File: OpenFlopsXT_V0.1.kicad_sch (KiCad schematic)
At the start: 69 parts, among them J1 UP, J2 DN, J3 R, J4 G, J5 Conn_01x22_Female, P1 FLOPPY_CONN, P2 POWER_INPUT, P3 POWER_PASSTHRU, P4 PROG_PORT, P6 ENCODER_PORT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

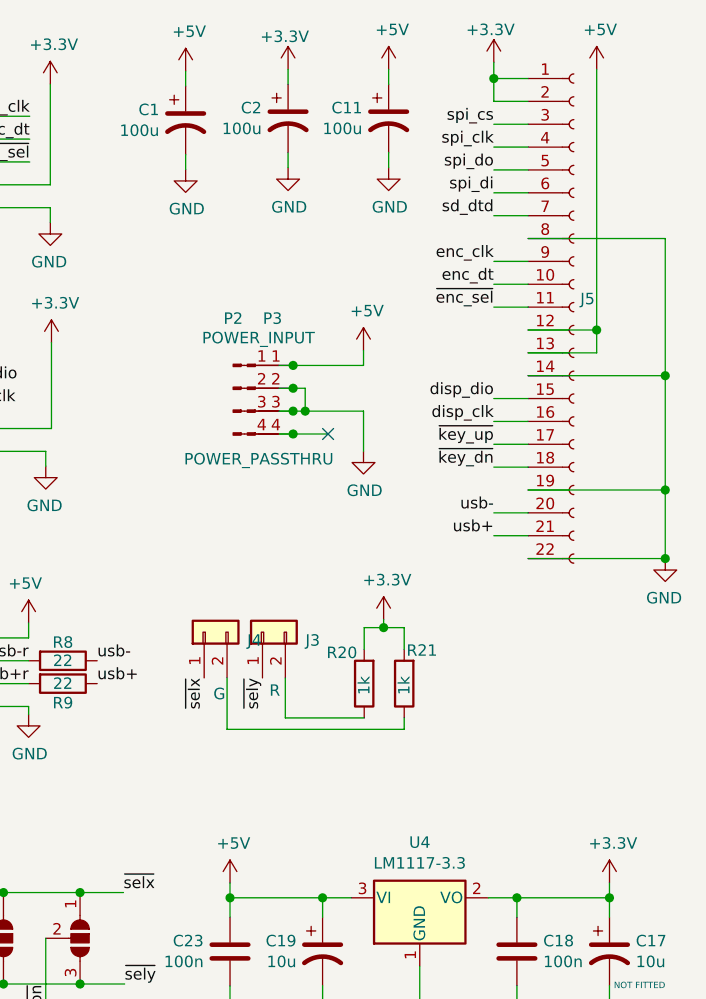
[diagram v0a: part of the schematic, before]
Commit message: Upgraded Flat Flex Connector OpenFlopsXT
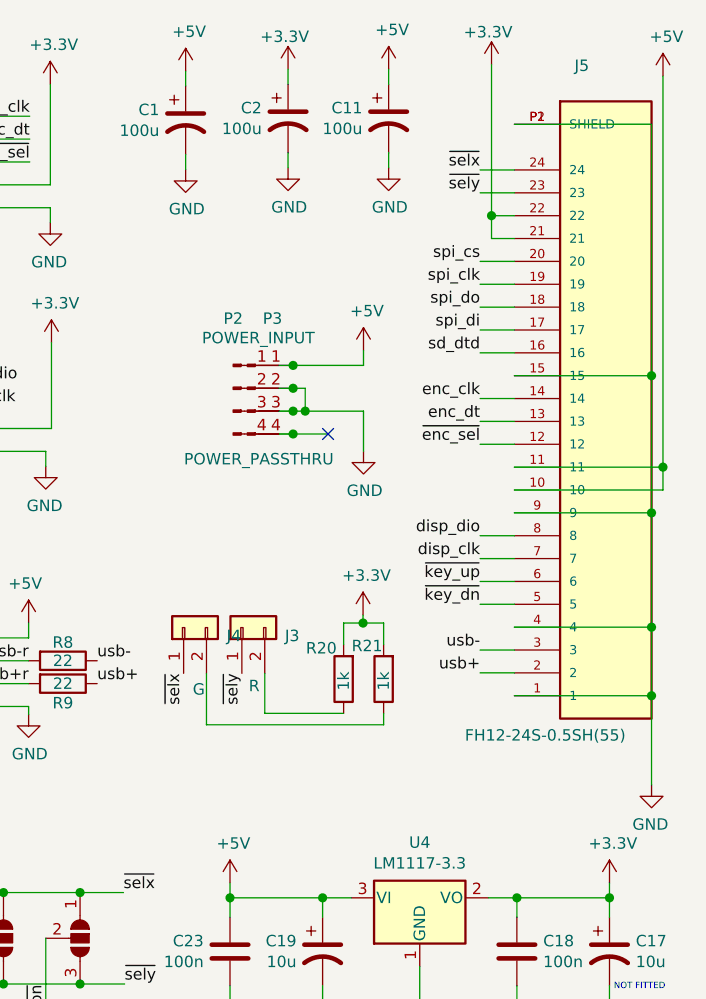
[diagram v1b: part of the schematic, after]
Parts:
- removed J5: Conn_01x22_Female, CM4IO:Hirose_FH12-22S-0.5SH_1x22-1MP_P0.50mm_Horizontal, symbol Connector:Conn_01x22_Female
- added J5: FH12-24S-0.5SH(55), OpenFlops:HRS_FH12-24S-0.5SH(55), symbol OpenFlops:FH12-24S-0.5SH(55)
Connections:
- net +3V3: now also J5.21, J5.22
- net +5V: now also J5.10, J5.11
- net GND: now also J5.1, J5.15, J5.4, J5.9, J5.P1 (SHIELD), J5.P2 (SHIELD)
- net disp_clk: now also J5.7
- net disp_dio: now also J5.8
- net enc_clk: now also J5.14
- net enc_dt: now also J5.13
- net sd_dtd: now also J5.16
- net spi_clk: now also J5.19
- net spi_cs: now also J5.20
- net spi_di: now also J5.17
- net spi_do: now also J5.18
- net usb+: now also J5.2
- net usb-: now also J5.3
- net ~{enc_sel}: now also J5.12
- net ~{key_dn}: now also J5.5
- net ~{key_up}: now also J5.6
- net ~{selx}: now also J5.24
- net ~{sely}: now also J5.23
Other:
- moved on the sheet: J3, J4, R20, R21

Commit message: Tidy up OpenFlopsXT for manufature
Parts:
- removed P3: POWER_PASSTHRU, OpenFlops:PinHeader_1x04_P2.54mm_Vertical_Power, symbol Connector:Conn_01x04_Male
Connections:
- net +3V3: now also C1.1, P6.5 (Pin_5); no longer P6.2 (Pin_2)
- net +5V: no longer C1.1
- net enc_clk: now also P6.4 (Pin_4); no longer P6.5 (Pin_5)
- net enc_dt: now also P6.3 (Pin_3); no longer P6.4 (Pin_4)
- net ~{enc_sel}: now also P6.2 (Pin_2); no longer P6.3 (Pin_3)
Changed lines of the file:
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@@
   (junction (at 217.17 120.6754) (diameter 1.016) (color 0 0 0 0))
   (junction (at 233.8324 111.0996) (diameter 1.016) (color 0 0 0 0))
-  (junction (at 240.8427 51.943) (diameter 1.016) (color 0 0 0 0))
-  (junction (at 240.8427 54.483) (diameter 1.016) (color 0 0 0 0))
-  (junction (at 240.8427 57.023) (diameter 1.016) (color 0 0 0 0))
-  (junction (at 240.8427 59.563) (diameter 1.016) (color 0 0 0 0))
   (junction (at 242.189 57.023) (diameter 1.016) (color 0 0 0 0))
   (junction (at 244.0686 132.207) (diameter 1.016) (color 0 0 0 0))
@@
     (stroke (width 0) (type solid) (color 0 0 0 0))
   )
-  (wire (pts (xy 203.962 24.257) (xy 211.582 24.257))
+  (wire (pts (xy 203.962 24.257) (xy 213.868 24.257))
     (stroke (width 0) (type solid) (color 0 0 0 0))
   )
@@
     (stroke (width 0) (type solid) (color 0 0 0 0))
   )
-  (wire (pts (xy 203.962 31.877) (xy 213.868 31.877))
+  (wire (pts (xy 203.962 31.877) (xy 211.582 31.877))
     (stroke (width 0) (type solid) (color 0 0 0 0))
   )
@@
     (stroke (width 0) (type solid) (color 0 0 0 0))
   )
-  (wire (pts (xy 213.868 31.877) (xy 213.868 20.701))
+  (wire (pts (xy 213.868 24.257) (xy 213.868 20.701))
     (stroke (width 0) (type solid) (color 0 0 0 0))
   )
@@
     (stroke (width 0) (type solid) (color 0 0 0 0))
   )
-  (wire (pts (xy 239.268 51.943) (xy 240.8427 51.943))
+  (wire (pts (xy 239.268 51.943) (xy 248.666 51.943))
     (stroke (width 0) (type solid) (color 0 0 0 0))
   )
-  (wire (pts (xy 239.268 54.483) (xy 240.8427 54.483))
+  (wire (pts (xy 239.268 54.483) (xy 242.189 54.483))
     (stroke (width 0) (type solid) (color 0 0 0 0))
   )
-  (wire (pts (xy 239.268 57.023) (xy 240.8427 57.023))
+  (wire (pts (xy 239.268 57.023) (xy 242.189 57.023))
     (stroke (width 0) (type solid) (color 0 0 0 0))
   )
-  (wire (pts (xy 239.268 59.563) (xy 240.8427 59.563))
+  (wire (pts (xy 239.268 59.563) (xy 244.729 59.563))
     (stroke (width 0) (type solid) (color 0 0 0 0))
   )
@@
     (stroke (width 0) (type solid) (color 0 0 0 0))
   )
-  (wire (pts (xy 240.8427 51.943) (xy 248.666 51.943))
-    (stroke (width 0) (type solid) (color 0 0 0 0))
-  )
-  (wire (pts (xy 240.8427 54.483) (xy 242.189 54.483))
-    (stroke (width 0) (type solid) (color 0 0 0 0))
-  )
-  (wire (pts (xy 240.8427 57.023) (xy 242.189 57.023))
-    (stroke (width 0) (type solid) (color 0 0 0 0))
-  )
-  (wire (pts (xy 240.8427 59.563) (xy 244.729 59.563))
-    (stroke (width 0) (type solid) (color 0 0 0 0))
-  )
   (wire (pts (xy 242.189 54.483) (xy 242.189 57.023))
     (stroke (width 0) (type solid) (color 0 0 0 0))
@@
     (effects (font (size 1.27 1.27)) (justify right bottom))
   )
-  (label "enc_clk" (at 211.582 24.257 180)
+  (label "enc_clk" (at 211.582 26.797 180)
     (effects (font (size 1.27 1.27)) (justify right bottom))
   )
-  (label "enc_dt" (at 211.582 26.797 180)
+  (label "enc_dt" (at 211.582 29.337 180)
     (effects (font (size 1.27 1.27)) (justify right bottom))
   )
-  (label "~{enc_sel}" (at 211.582 29.337 180)
+  (label "~{enc_sel}" (at 211.582 31.877 180)
     (effects (font (size 1.27 1.27)) (justify right bottom))
   )
@@
     (pin "1")
   )
-  (symbol (lib_id "power:+5V") (at 228.9048 19.2532 0) (unit 1)
+  (symbol (lib_id "power:+3.3V") (at 228.9048 19.2532 0) (unit 1)
     (in_bom yes) (on_board yes)
-    (property "Reference" "#PWR0141" (id 0) (at 228.9048 23.0632 0)
+    (property "Reference" "#PWR?" (id 0) (at 228.9048 23.0632 0)
       (effects (font (size 1.27 1.27)) hide)
     )
-    (property "Value" "+5V" (id 1) (at 229.2858 14.859 0))
+    (property "Value" "+3.3V" (id 1) (at 228.5238 15.621 0))
     (property "Footprint" "" (id 2) (at 228.9048 19.2532 0)
       (effects (font (size 1.27 1.27)) hide)
@@
     (pin "4")
   )
-  (symbol (lib_id "Connector:Conn_01x04_Male") (at 235.7627 54.483 0) (unit 1)
-    (in_bom yes) (on_board yes)
-    (property "Reference" "P3" (id 0) (at 238.5567 46.736 0))
-    (property "Value" "POWER_PASSTHRU" (id 1) (at 237.0327 62.357 0))
-    (property "Footprint" "OpenFlops:PinHeader_1x04_P2.54mm_Vertical_Power" (id 2) (at 235.7627 54.483 0)
-      (effects (font (size 1.27 1.27)) hide)
-    )
-    (property "Datasheet" "~" (id 3) (at 235.7627 54.483 0)
-      (effects (font (size 1.27 1.27)) hide)
-    )
-    (pin "1")
-    (pin "2")
-    (pin "3")
-    (pin "4")
-  )
   (symbol (lib_id "OpenFlops-rescue:MOS_N_GSD-w_transistor") (at 77.216 141.986 0) (unit 1)
     (in_bom yes) (on_board yes)
@@
       (reference "#PWR0140") (unit 1) (value "+3.3V") (footprint "")
     )
-    (path "/00000000-0000-0000-0000-00005ee997a6"
-      (reference "#PWR0141") (unit 1) (value "+5V") (footprint "")
-    )
     (path "/00000000-0000-0000-0000-00005eec2a25"
       (reference "#PWR0142") (unit 1) (value "GND") (footprint "")
@@
       (reference "#PWR0146") (unit 1) (value "GND") (footprint "")
     )
+    (path "/0c60f8df-a7d2-4829-a86f-6dfcb6797044"
+      (reference "#PWR?") (unit 1) (value "+3.3V") (footprint "")
+    )
     (path "/00000000-0000-0000-0000-00005ee6c285"
       (reference "C1") (unit 1) (value "100u") (footprint "Jumper:SolderJumper-2_P1.3mm_Open_RoundedPad1.0x1.5mm")
@@
       (reference "P2") (unit 1) (value "POWER_INPUT") (footprint "OpenFlops:PinHeader_1x04_P2.54mm_Vertical_Power")
     )
-    (path "/14b9ca32-ed51-4d62-9aa8-177fb0615c81"
-      (reference "P3") (unit 1) (value "POWER_PASSTHRU") (footprint "OpenFlops:PinHeader_1x04_P2.54mm_Vertical_Power")
-    )
     (path "/00000000-0000-0000-0000-00005d4fbc5b"

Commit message: Correct missing pin 1 locators and Tidy up OpenfFLopsXT
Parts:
- added P3: POWER_PASSTHRU, OpenFlops:PinHeader_1x04_P2.54mm_Vertical_Power, symbol Connector:Conn_01x04_Male
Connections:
- net +3V3: now also P6.2 (Pin_2); no longer C1.1, P6.5 (Pin_5)
- net +5V: now also C1.1, P3.1 (Pin_1)
- net GND: now also P3.2 (Pin_2), P3.3 (Pin_3)
- net enc_clk: now also P6.5 (Pin_5); no longer P6.4 (Pin_4)
- net enc_dt: now also P6.4 (Pin_4); no longer P6.3 (Pin_3)
- net ~{enc_sel}: now also P6.3 (Pin_3); no longer P6.2 (Pin_2)
- net at P2.4 (Pin_4): now also P3.4 (Pin_4)
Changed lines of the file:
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@@
   (junction (at 217.17 120.6754) (diameter 1.016) (color 0 0 0 0))
   (junction (at 233.8324 111.0996) (diameter 1.016) (color 0 0 0 0))
+  (junction (at 240.8427 51.943) (diameter 1.016) (color 0 0 0 0))
+  (junction (at 240.8427 54.483) (diameter 1.016) (color 0 0 0 0))
+  (junction (at 240.8427 57.023) (diameter 1.016) (color 0 0 0 0))
+  (junction (at 240.8427 59.563) (diameter 1.016) (color 0 0 0 0))
   (junction (at 242.189 57.023) (diameter 1.016) (color 0 0 0 0))
   (junction (at 244.0686 132.207) (diameter 1.016) (color 0 0 0 0))
@@
     (stroke (width 0) (type solid) (color 0 0 0 0))
   )
-  (wire (pts (xy 203.962 24.257) (xy 213.868 24.257))
+  (wire (pts (xy 203.962 24.257) (xy 211.582 24.257))
     (stroke (width 0) (type solid) (color 0 0 0 0))
   )
@@
     (stroke (width 0) (type solid) (color 0 0 0 0))
   )
-  (wire (pts (xy 203.962 31.877) (xy 211.582 31.877))
+  (wire (pts (xy 203.962 31.877) (xy 213.868 31.877))
     (stroke (width 0) (type solid) (color 0 0 0 0))
   )
@@
     (stroke (width 0) (type solid) (color 0 0 0 0))
   )
-  (wire (pts (xy 213.868 24.257) (xy 213.868 20.701))
+  (wire (pts (xy 213.868 31.877) (xy 213.868 20.701))
     (stroke (width 0) (type solid) (color 0 0 0 0))
   )
@@
     (stroke (width 0) (type solid) (color 0 0 0 0))
   )
-  (wire (pts (xy 239.268 51.943) (xy 248.666 51.943))
+  (wire (pts (xy 239.268 51.943) (xy 240.8427 51.943))
     (stroke (width 0) (type solid) (color 0 0 0 0))
   )
-  (wire (pts (xy 239.268 54.483) (xy 242.189 54.483))
+  (wire (pts (xy 239.268 54.483) (xy 240.8427 54.483))
     (stroke (width 0) (type solid) (color 0 0 0 0))
   )
-  (wire (pts (xy 239.268 57.023) (xy 242.189 57.023))
+  (wire (pts (xy 239.268 57.023) (xy 240.8427 57.023))
     (stroke (width 0) (type solid) (color 0 0 0 0))
   )
-  (wire (pts (xy 239.268 59.563) (xy 244.729 59.563))
+  (wire (pts (xy 239.268 59.563) (xy 240.8427 59.563))
     (stroke (width 0) (type solid) (color 0 0 0 0))
   )
@@
     (stroke (width 0) (type solid) (color 0 0 0 0))
   )
+  (wire (pts (xy 240.8427 51.943) (xy 248.666 51.943))
+    (stroke (width 0) (type solid) (color 0 0 0 0))
+  )
+  (wire (pts (xy 240.8427 54.483) (xy 242.189 54.483))
+    (stroke (width 0) (type solid) (color 0 0 0 0))
+  )
+  (wire (pts (xy 240.8427 57.023) (xy 242.189 57.023))
+    (stroke (width 0) (type solid) (color 0 0 0 0))
+  )
+  (wire (pts (xy 240.8427 59.563) (xy 244.729 59.563))
+    (stroke (width 0) (type solid) (color 0 0 0 0))
+  )
   (wire (pts (xy 242.189 54.483) (xy 242.189 57.023))
     (stroke (width 0) (type solid) (color 0 0 0 0))
@@
     (effects (font (size 1.27 1.27)) (justify right bottom))
   )
-  (label "enc_clk" (at 211.582 26.797 180)
+  (label "enc_clk" (at 211.582 24.257 180)
     (effects (font (size 1.27 1.27)) (justify right bottom))
   )
-  (label "enc_dt" (at 211.582 29.337 180)
+  (label "enc_dt" (at 211.582 26.797 180)
     (effects (font (size 1.27 1.27)) (justify right bottom))
   )
-  (label "~{enc_sel}" (at 211.582 31.877 180)
+  (label "~{enc_sel}" (at 211.582 29.337 180)
     (effects (font (size 1.27 1.27)) (justify right bottom))
   )
@@
     (pin "1")
   )
-  (symbol (lib_id "power:+3.3V") (at 228.9048 19.2532 0) (unit 1)
+  (symbol (lib_id "power:+5V") (at 228.9048 19.2532 0) (unit 1)
     (in_bom yes) (on_board yes)
-    (property "Reference" "#PWR?" (id 0) (at 228.9048 23.0632 0)
+    (property "Reference" "#PWR0141" (id 0) (at 228.9048 23.0632 0)
       (effects (font (size 1.27 1.27)) hide)
     )
-    (property "Value" "+3.3V" (id 1) (at 228.5238 15.621 0))
+    (property "Value" "+5V" (id 1) (at 229.2858 14.859 0))
     (property "Footprint" "" (id 2) (at 228.9048 19.2532 0)
       (effects (font (size 1.27 1.27)) hide)
@@
     (pin "4")
   )
+  (symbol (lib_id "Connector:Conn_01x04_Male") (at 235.7627 54.483 0) (unit 1)
+    (in_bom yes) (on_board yes)
+    (property "Reference" "P3" (id 0) (at 238.5567 46.736 0))
+    (property "Value" "POWER_PASSTHRU" (id 1) (at 237.0327 62.357 0))
+    (property "Footprint" "OpenFlops:PinHeader_1x04_P2.54mm_Vertical_Power" (id 2) (at 235.7627 54.483 0)
+      (effects (font (size 1.27 1.27)) hide)
+    )
+    (property "Datasheet" "~" (id 3) (at 235.7627 54.483 0)
+      (effects (font (size 1.27 1.27)) hide)
+    )
+    (pin "1")
+    (pin "2")
+    (pin "3")
+    (pin "4")
+  )
   (symbol (lib_id "OpenFlops-rescue:MOS_N_GSD-w_transistor") (at 77.216 141.986 0) (unit 1)
     (in_bom yes) (on_board yes)
@@
       (reference "#PWR0140") (unit 1) (value "+3.3V") (footprint "")
     )
+    (path "/00000000-0000-0000-0000-00005ee997a6"
+      (reference "#PWR0141") (unit 1) (value "+5V") (footprint "")
+    )
     (path "/00000000-0000-0000-0000-00005eec2a25"
       (reference "#PWR0142") (unit 1) (value "GND") (footprint "")
@@
       (reference "#PWR0146") (unit 1) (value "GND") (footprint "")
     )
-    (path "/0c60f8df-a7d2-4829-a86f-6dfcb6797044"
-      (reference "#PWR?") (unit 1) (value "+3.3V") (footprint "")
-    )
     (path "/00000000-0000-0000-0000-00005ee6c285"
       (reference "C1") (unit 1) (value "100u") (footprint "Jumper:SolderJumper-2_P1.3mm_Open_RoundedPad1.0x1.5mm")
@@
       (reference "P2") (unit 1) (value "POWER_INPUT") (footprint "OpenFlops:PinHeader_1x04_P2.54mm_Vertical_Power")
     )
+    (path "/14b9ca32-ed51-4d62-9aa8-177fb0615c81"
+      (reference "P3") (unit 1) (value "POWER_PASSTHRU") (footprint "OpenFlops:PinHeader_1x04_P2.54mm_Vertical_Power")
+    )
     (path "/00000000-0000-0000-0000-00005d4fbc5b"

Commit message: Retreve from backup due to git error
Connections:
- net +3V3: now also C1.1, P6.5 (Pin_5); no longer P6.2 (Pin_2)
- net +5V: no longer C1.1
- net enc_clk: now also P6.4 (Pin_4); no longer P6.5 (Pin_5)
- net enc_dt: now also P6.3 (Pin_3); no longer P6.4 (Pin_4)
- net ~{enc_sel}: now also P6.2 (Pin_2); no longer P6.3 (Pin_3)
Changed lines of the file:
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@@
     (stroke (width 0) (type solid) (color 0 0 0 0))
   )
-  (wire (pts (xy 203.962 24.257) (xy 211.582 24.257))
+  (wire (pts (xy 203.962 24.257) (xy 213.868 24.257))
     (stroke (width 0) (type solid) (color 0 0 0 0))
   )
@@
     (stroke (width 0) (type solid) (color 0 0 0 0))
   )
-  (wire (pts (xy 203.962 31.877) (xy 213.868 31.877))
+  (wire (pts (xy 203.962 31.877) (xy 211.582 31.877))
     (stroke (width 0) (type solid) (color 0 0 0 0))
   )
@@
     (stroke (width 0) (type solid) (color 0 0 0 0))
   )
-  (wire (pts (xy 213.868 31.877) (xy 213.868 20.701))
+  (wire (pts (xy 213.868 24.257) (xy 213.868 20.701))
     (stroke (width 0) (type solid) (color 0 0 0 0))
   )
@@
     (effects (font (size 1.27 1.27)) (justify right bottom))
   )
-  (label "enc_clk" (at 211.582 24.257 180)
+  (label "enc_clk" (at 211.582 26.797 180)
     (effects (font (size 1.27 1.27)) (justify right bottom))
   )
-  (label "enc_dt" (at 211.582 26.797 180)
+  (label "enc_dt" (at 211.582 29.337 180)
     (effects (font (size 1.27 1.27)) (justify right bottom))
   )
-  (label "~{enc_sel}" (at 211.582 29.337 180)
+  (label "~{enc_sel}" (at 211.582 31.877 180)
     (effects (font (size 1.27 1.27)) (justify right bottom))
   )
@@
     (pin "1")
   )
-  (symbol (lib_id "power:+5V") (at 228.9048 19.2532 0) (unit 1)
+  (symbol (lib_id "power:+3.3V") (at 228.9048 19.2532 0) (unit 1)
     (in_bom yes) (on_board yes)
-    (property "Reference" "#PWR0141" (id 0) (at 228.9048 23.0632 0)
+    (property "Reference" "#PWR?" (id 0) (at 228.9048 23.0632 0)
       (effects (font (size 1.27 1.27)) hide)
     )
-    (property "Value" "+5V" (id 1) (at 229.2858 14.859 0))
+    (property "Value" "+3.3V" (id 1) (at 228.5238 15.621 0))
     (property "Footprint" "" (id 2) (at 228.9048 19.2532 0)
       (effects (font (size 1.27 1.27)) hide)
@@
       (reference "#PWR0140") (unit 1) (value "+3.3V") (footprint "")
     )
-    (path "/00000000-0000-0000-0000-00005ee997a6"
-      (reference "#PWR0141") (unit 1) (value "+5V") (footprint "")
-    )
     (path "/00000000-0000-0000-0000-00005eec2a25"
       (reference "#PWR0142") (unit 1) (value "GND") (footprint "")
@@
       (reference "#PWR0146") (unit 1) (value "GND") (footprint "")
     )
+    (path "/0c60f8df-a7d2-4829-a86f-6dfcb6797044"
+      (reference "#PWR?") (unit 1) (value "+3.3V") (footprint "")
+    )
     (path "/00000000-0000-0000-0000-00005ee6c285"
